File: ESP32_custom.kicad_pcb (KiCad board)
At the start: 4 copper layers, 32 x 42.2 mm, 28 parts, among them J1 TYPE-C-31-M-12, J2 Conn_01x16_Pin, J3 Conn_01x16_Pin, Q1 SS8050, Q2 SS8050, SW1 SW_Push, SW2 SW_Push, U2 ESP32-WROOM-32E 8MB, U3 CH340C, U4 AMS1117-3.3

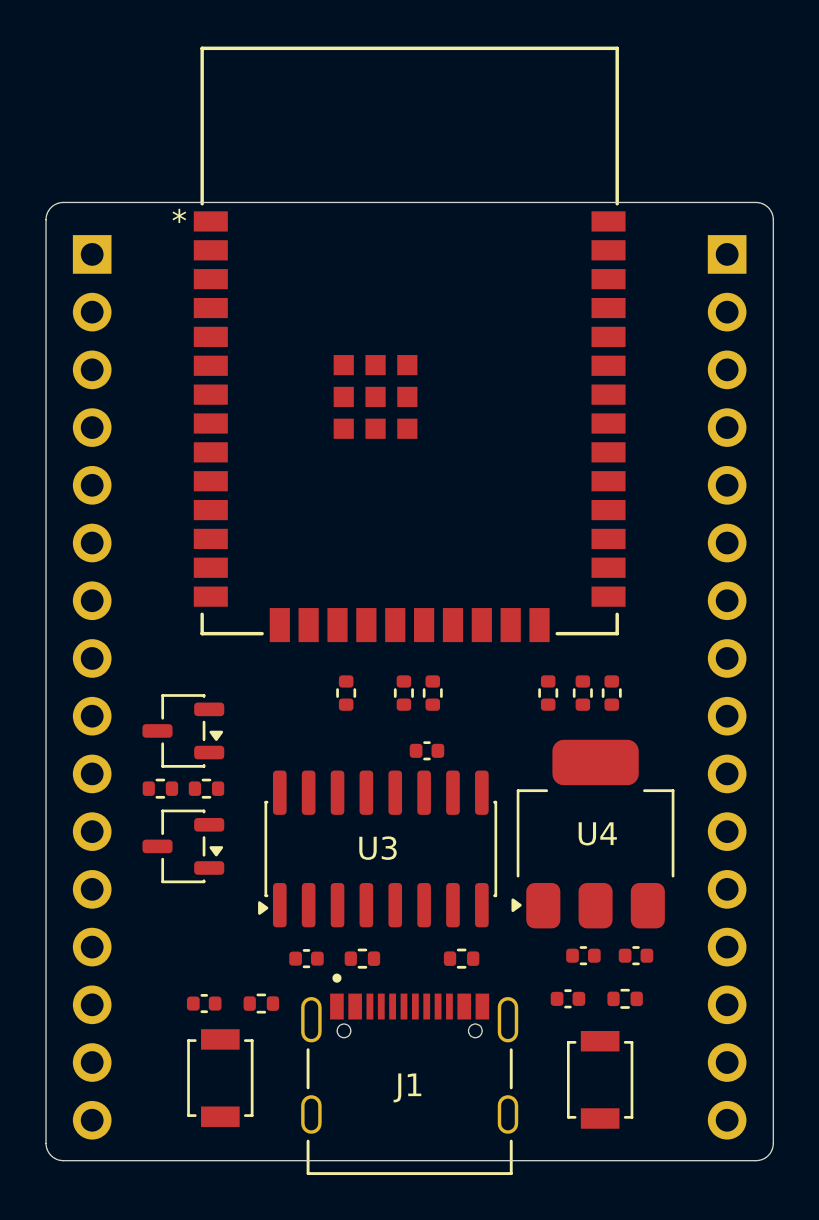
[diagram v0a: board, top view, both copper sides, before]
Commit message: finish routing (DRC fail)
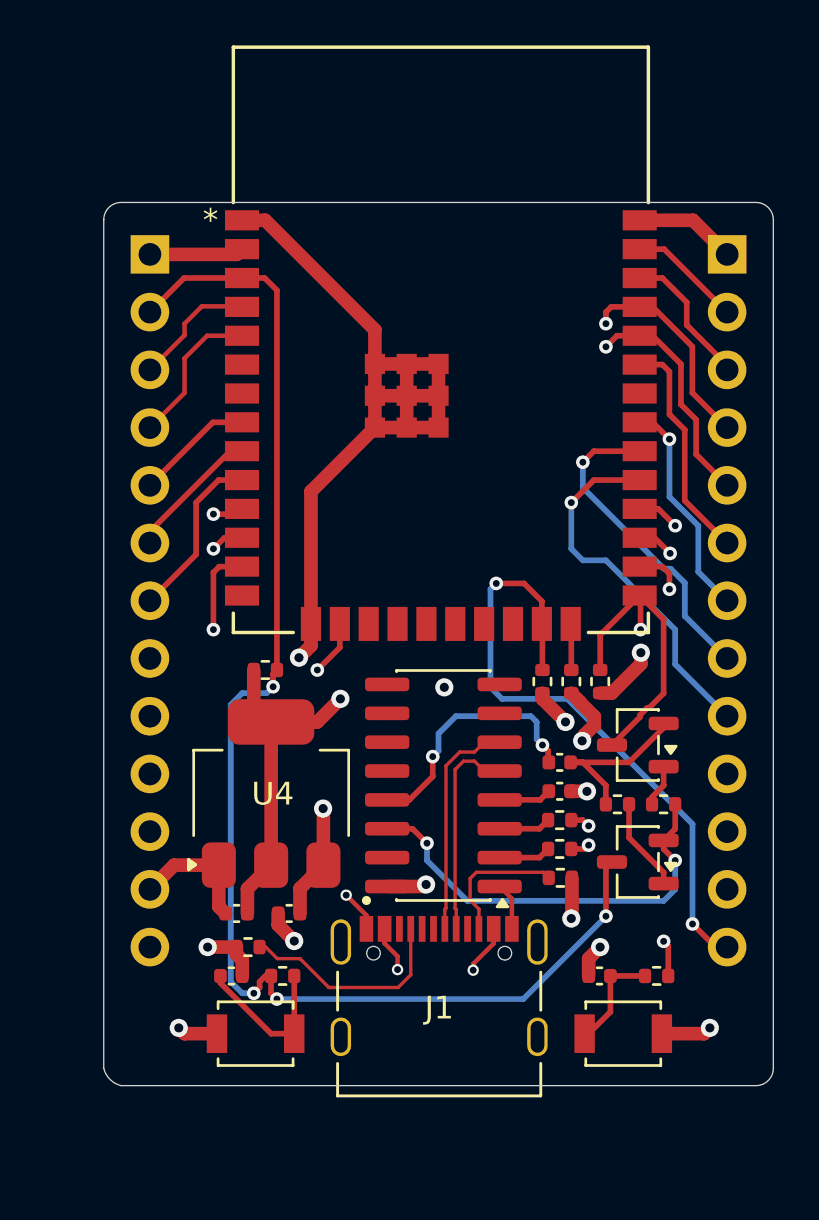
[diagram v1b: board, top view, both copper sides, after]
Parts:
- J2, J3: value Conn_01x16_Pin -> Conn_01x13_Pin; footprint Connector_PinHeader_2.54mm:PinHeader_1x16_P2.54mm_Vertical -> Connector_PinHeader_2.54mm:PinHeader_1x13_P2.54mm_Vertical
- moved R8 20.1 mm to (139.4, 87.2)
- moved R7 20.1 mm to (137.4, 87.2)
- moved Q1 20.0 mm to (138.3, 89.7)
- moved Q2 20.0 mm to (138.3, 84.6)
- moved C3 15.4 mm to (120.7, 92.0)
- moved C4 15.4 mm to (123.0, 92.0)
- moved U4 14.4 mm to (122.2, 86.7)
- moved C2 13.4 mm to (134.9, 86.6)
- moved R2 9.70 mm to (134.9, 89.2), turned to 0 degrees
- moved R1 7.90 mm to (134.9, 87.9), turned to 0 degrees
- moved C1 5.86 mm to (134.9, 85.3), turned to 0 degrees
- moved R11 5.61 mm to (134.9, 90.4)
- moved R12 5.06 mm to (121.2, 93.5)
- moved U3 3.92 mm to (129.8, 86.4), turned to 180 degrees
- moved R9 3.70 mm to (121.9, 81.3), turned to 0 degrees
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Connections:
- J2 pad 10: /IO26 -> /IO14
- J2 pad 11: /IO27 -> /IO13
- J2 pad 12: /IO14 -> GND
- J2 pad 13: /IO12 -> +5V
- J2 pad 5: /IO34 -> /IO32
- J2 pad 6: /IO35 -> /IO33
- J2 pad 7: /IO32 -> /IO25
- J2 pad 8: /IO33 -> /IO26
- J2 pad 9: /IO25 -> /IO27
- J3 pad 10: /IO5 -> /IO17
- J3 pad 11: /IO17 -> /IO16
- J3 pad 12: /IO16 -> /IO4
- J3 pad 13: /IO4 -> /IO15
- J3 pad 7: GND -> /IO19
- J3 pad 8: /IO19 -> /IO18
- J3 pad 9: /IO18 -> /IO5
- U2 pad 14: /IO12 -> unconnected-(U2-IO12-Pad14)
- U2 pad 6: /IO34 -> unconnected-(U2-IO34-Pad6)
- U2 pad 7: /IO35 -> unconnected-(U2-IO35-Pad7)
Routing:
- net GND: track 0.00 -> 68.4 mm, vias 0 -> 11
- net /EN: track 0.00 -> 60.4 mm, vias 0 -> 4
- net /RX: track 0.00 -> 34.4 mm, vias 0 -> 2
- net VCC: track 0.00 -> 33.5 mm, vias 0 -> 4
- net /TX: track 0.00 -> 32.8 mm, vias 0 -> 2
- net /IO0: track 0.00 -> 29.3 mm, vias 0 -> 2
- net /IO15: track 0.00 -> 27.8 mm, vias 0 -> 2
- net /RTS: track 0.00 -> 18.8 mm, vias 0 -> 2
- net /IO4: track 0.00 -> 16.4 mm, vias 0 -> 1
- net /IO5: track 0.00 -> 16.3 mm, vias 0 -> 1
- net /IO16: track 0.00 -> 14.9 mm, vias 0 -> 1
- net /IO18: track 0.00 -> 14.1 mm, vias 0 -> 1
- net /IO17: track 0.00 -> 13.7 mm, vias 0 -> 1
- net /IO13: track 0.00 -> 12.8 mm, vias 0 -> 1
- net /IO14: track 0.00 -> 11.4 mm, vias 0 -> 1
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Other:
- board size 32 x 42.2 mm -> 29.5 x 38.9 mm

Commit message: update schematic. changed to esp32-s3
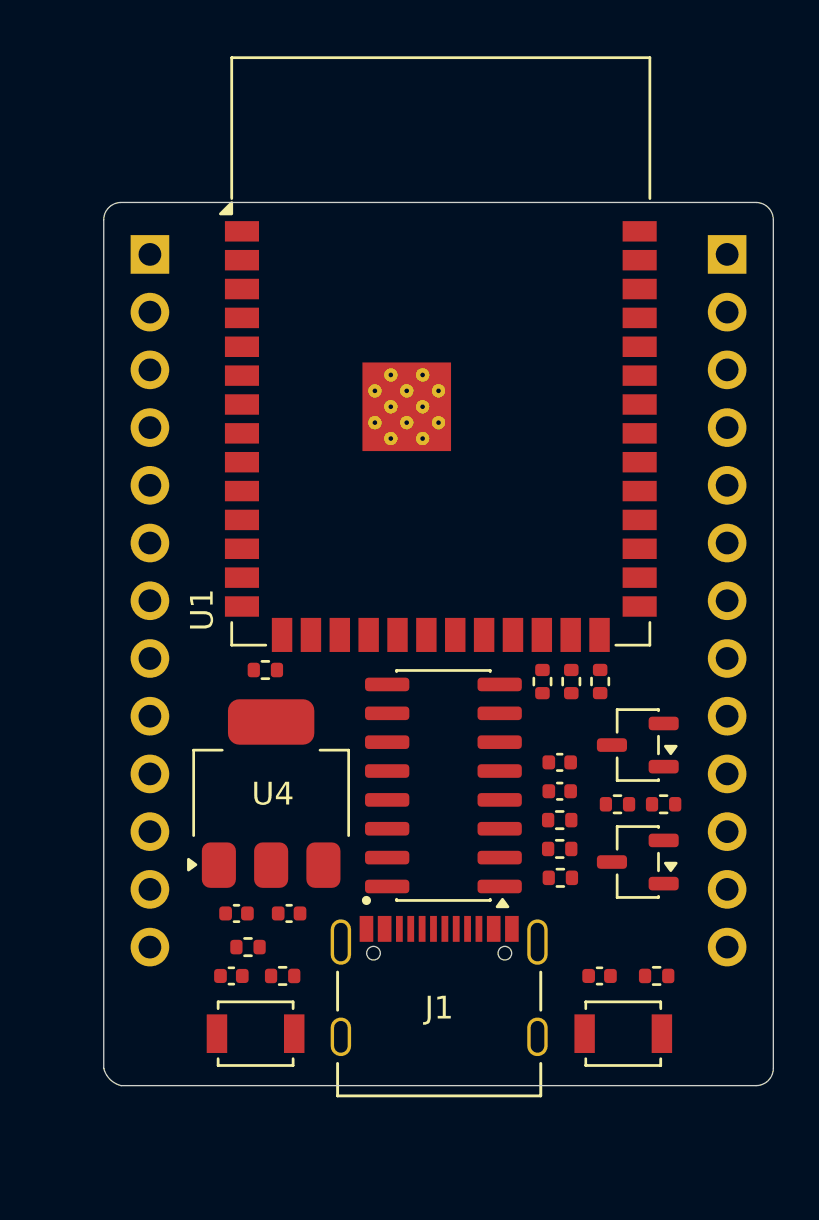
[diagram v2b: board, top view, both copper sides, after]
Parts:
- removed U2: ESP32-WROOM-32E 8MB, KiCADv6:ESP32­WROOM­32E_EXP
- added U1: ESP32-S3-WROOM-1, RF_Module:ESP32-S3-WROOM-1, F.Cu at (129.6, 67.2)
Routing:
- net GND: track 68.4 -> 0.00 mm, vias 11 -> 0
- net /EN: track 60.4 -> 0.00 mm, vias 4 -> 0
- net /RX: track 34.4 -> 0.00 mm, vias 2 -> 0
- net VCC: track 33.5 -> 0.00 mm, vias 4 -> 0
- net /TX: track 32.8 -> 0.00 mm, vias 2 -> 0
- net /IO0: track 29.3 -> 0.00 mm, vias 2 -> 0
- net /IO15: track 27.8 -> 0.00 mm, vias 2 -> 0
- net /RTS: track 18.8 -> 0.00 mm, vias 2 -> 0
- net /IO4: track 16.4 -> 0.00 mm, vias 1 -> 0
- net /IO5: track 16.3 -> 0.00 mm, vias 1 -> 0
- net /IO16: track 14.9 -> 0.00 mm, vias 1 -> 0
- net /IO18: track 14.1 -> 0.00 mm, vias 1 -> 0
- net /IO17: track 13.7 -> 0.00 mm, vias 1 -> 0
- net /IO13: track 12.8 -> 0.00 mm, vias 1 -> 0
- net /IO14: track 11.4 -> 0.00 mm, vias 1 -> 0
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
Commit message: update pcb
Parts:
- removed Q1, Q2: SS8050, Package_TO_SOT_SMD:SOT-23-3
- removed R10, R7, R8, R9: 10K, Resistor_SMD:R_0402_1005Metric
- removed R11, R12: 5.1K, Resistor_SMD:R_0402_1005Metric
- removed U3: CH340C, Package_SO:SOIC-16_3.9x9.9mm_P1.27mm
- added C10: 1uF, Capacitor_SMD:C_0402_1005Metric, F.Cu at (128.3, 90.2)
- added C7: 0u1F, Capacitor_SMD:C_0402_1005Metric, F.Cu at (128.3, 84.2)
- added C8: 10uF, Capacitor_SMD:C_0402_1005Metric, F.Cu at (128.3, 86.2)
- added C9: 10uF, Capacitor_SMD:C_0402_1005Metric, F.Cu at (128.3, 88.2)
- added D1: LESD5D5.0CT1G, LESD5D:TVS_LESD5D5.0CT1G, F.Cu at (137.4, 91.1)
- added D2: LESD5D5.0CT1G, LESD5D:TVS_LESD5D5.0CT1G, F.Cu at (137.4, 93.5)
- added D3: LESD5D5.0CT1G, LESD5D:TVS_LESD5D5.0CT1G, F.Cu at (137.4, 95.8)
- added D4: 1N5819HW-7-F, ul_1N5819HW-7-F:1N5819HW-7-F_DIO, F.Cu at (138.2, 84.1)
- added D5: LED, LED_SMD:LED_0201_0603Metric, F.Cu at (131.2, 84.1)
- added R13: 10K, Resistor_SMD:R_0201_0603Metric, F.Cu at (131.0, 87.6)
- C1, C6: value 100nF -> 0u1F
- C2: value 100nF -> 10uF
- C3, C5: value 10uF -> 0u1F
- R1: value 1K -> 5.1K; footprint Resistor_SMD:R_0402_1005Metric -> Resistor_SMD:R_0201_0603Metric
- R2: value 1K -> 10K; footprint Resistor_SMD:R_0402_1005Metric -> Resistor_SMD:R_0201_0603Metric
- R3: value 470 -> 10K; footprint Resistor_SMD:R_0402_1005Metric -> Resistor_SMD:R_0201_0603Metric
- R4: value 470 -> 10k; footprint Resistor_SMD:R_0402_1005Metric -> Resistor_SMD:R_0201_0603Metric
- R5, R6: value 10K -> 5K1; footprint Resistor_SMD:R_0402_1005Metric -> Resistor_SMD:R_0201_0603Metric
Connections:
- C1 pad 1: Net-(U3-~{DTR}) -> +5V
- C1 pad 2: /DTR -> GND
- C2 pad 1: Net-(U3-V3) -> +5V
- C4 pad 1: GND -> VCC
- C4 pad 2: +5V -> GND
- C5 pad 1: Net-(C5-Pad1) -> /GPIO0
- C6 pad 1: Net-(C6-Pad1) -> /CHIP_PU
- J1 pad A4_B9: +5V -> VBUS
- J1 pad A5: /CC1 -> Net-(J1-CC1)
- J1 pad B4_A9: +5V -> VBUS
- J1 pad B5: /CC2 -> Net-(J1-CC2)
- J1 pad S1: unconnected-(J1-SHIELD-PadS1)_3 -> GND
- J1 pad S2: unconnected-(J1-SHIELD-PadS1)_2 -> GND
- J1 pad S3: unconnected-(J1-SHIELD-PadS1) -> GND
- J1 pad S4: unconnected-(J1-SHIELD-PadS1)_1 -> GND
- J2 pad 2: /EN -> /CHIP_PU
- R1 pad 1: Net-(U3-RXD) -> VCC
- R1 pad 2: /TX -> Net-(D5-A)
- R2 pad 1: Net-(U3-TXD) -> /CHIP_PU
- R2 pad 2: /RX -> /ESP_3V3
- R3 pad 1: /IO0 -> VCC
- R3 pad 2: Net-(C5-Pad1) -> /GPIO0
- R4 pad 1: /EN -> VCC
- R4 pad 2: Net-(C6-Pad1) -> /CHIP_PU
- R5 pad 1: /IO0 -> Net-(J1-CC2)
- R5 pad 2: VCC -> GND
- R6 pad 1: /IO2 -> Net-(J1-CC1)
- SW1 pad 1: Net-(C5-Pad1) -> /GPIO0
- SW2 pad 1: Net-(C6-Pad1) -> /CHIP_PU
- U1 pad 1: Net-(U1-GND-Pad1) -> GND
- U1 pad 10: unconnected-(U1-IO17-Pad10) -> /GPIO17
- U1 pad 11: unconnected-(U1-IO18-Pad11) -> /GPIO18
- U1 pad 12: unconnected-(U1-IO8-Pad12) -> /GPIO08
- U1 pad 13: unconnected-(U1-USB_D--Pad13) -> /D-
- U1 pad 14: unconnected-(U1-USB_D+-Pad14) -> /D+
- U1 pad 15: unconnected-(U1-IO3-Pad15) -> /GPIO03
- U1 pad 16: unconnected-(U1-IO46-Pad16) -> /GPIO46
- U1 pad 17: unconnected-(U1-IO9-Pad17) -> /GPIO09
- U1 pad 18: unconnected-(U1-IO10-Pad18) -> /GPIO10
- U1 pad 19: unconnected-(U1-IO11-Pad19) -> /GPIO11
- U1 pad 2: unconnected-(U1-3V3-Pad2) -> /ESP_3V3
- U1 pad 20: unconnected-(U1-IO12-Pad20) -> /GPIO12
- U1 pad 21: unconnected-(U1-IO13-Pad21) -> /GPIO13
- U1 pad 22: unconnected-(U1-IO14-Pad22) -> /GPIO14
- U1 pad 23: unconnected-(U1-IO21-Pad23) -> /GPIO21
- U1 pad 24: unconnected-(U1-IO47-Pad24) -> /GPIO47
- U1 pad 25: unconnected-(U1-IO48-Pad25) -> /GPIO48
- U1 pad 26: unconnected-(U1-IO45-Pad26) -> /GPIO45
- U1 pad 27: unconnected-(U1-IO0-Pad27) -> /GPIO0
- U1 pad 28: unconnected-(U1-IO35-Pad28) -> /GPIO35
- U1 pad 29: unconnected-(U1-IO36-Pad29) -> /GPIO36
- U1 pad 3: unconnected-(U1-EN-Pad3) -> /CHIP_PU
- U1 pad 30: unconnected-(U1-IO37-Pad30) -> /GPIO37
- U1 pad 31: unconnected-(U1-IO38-Pad31) -> /GPIO38
- U1 pad 32: unconnected-(U1-IO39-Pad32) -> /GPIO39
- U1 pad 33: unconnected-(U1-IO40-Pad33) -> /GPIO40
- U1 pad 34: unconnected-(U1-IO41-Pad34) -> /GPIO41
- U1 pad 35: unconnected-(U1-IO42-Pad35) -> /GPIO42
- U1 pad 36: unconnected-(U1-RXD0-Pad36) -> /RX
- U1 pad 37: unconnected-(U1-TXD0-Pad37) -> /TX
- U1 pad 38: unconnected-(U1-IO2-Pad38) -> /GPIO02
- U1 pad 39: unconnected-(U1-IO1-Pad39) -> /GPIO01
- U1 pad 4: unconnected-(U1-IO4-Pad4) -> /GPIO04
- U1 pad 40: Net-(U1-GND-Pad1) -> GND
- U1 pad 41: Net-(U1-GND-Pad1) -> GND
- U1 pad 5: unconnected-(U1-IO5-Pad5) -> /GPIO05
- U1 pad 6: unconnected-(U1-IO6-Pad6) -> /GPIO06
- U1 pad 7: unconnected-(U1-IO7-Pad7) -> /GPIO07
- U1 pad 8: unconnected-(U1-IO15-Pad8) -> /GPIO15
- U1 pad 9: unconnected-(U1-IO16-Pad9) -> /GPIO16

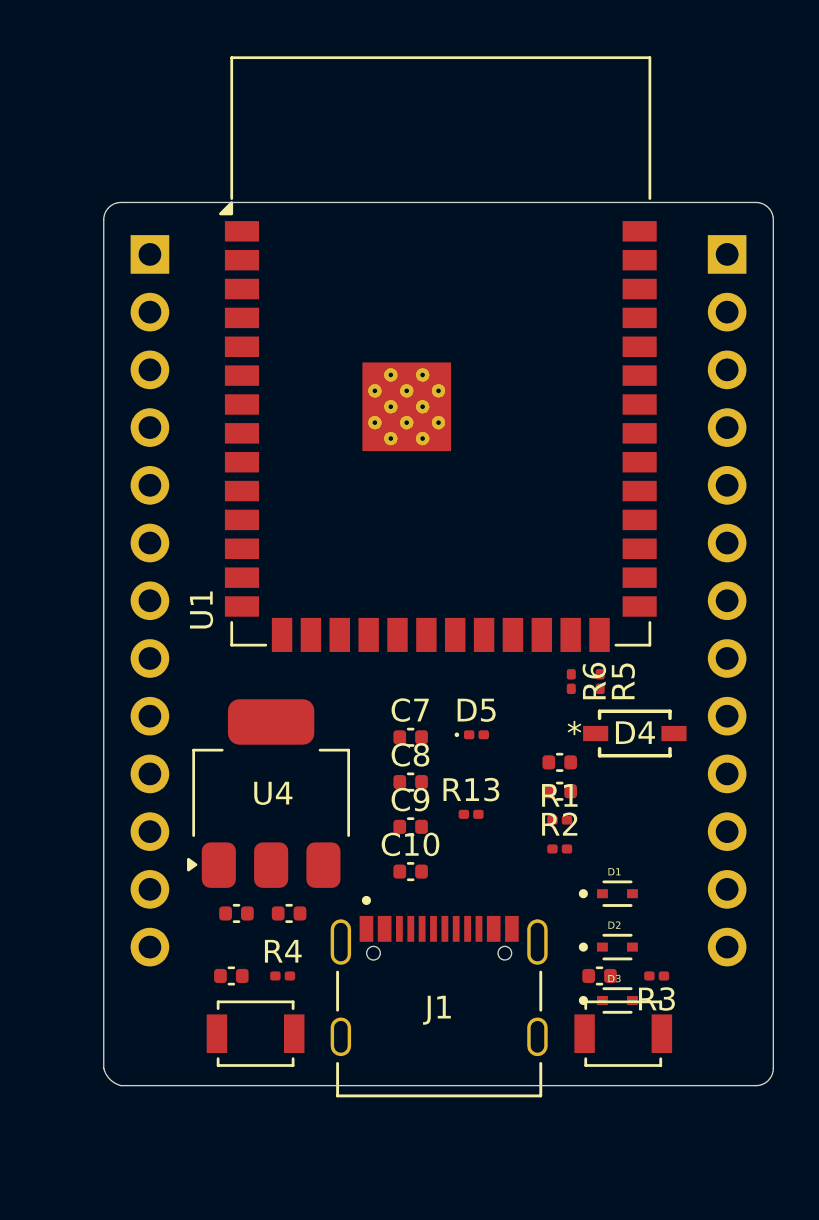
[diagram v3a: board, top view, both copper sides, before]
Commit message: arrange components and update pin header label
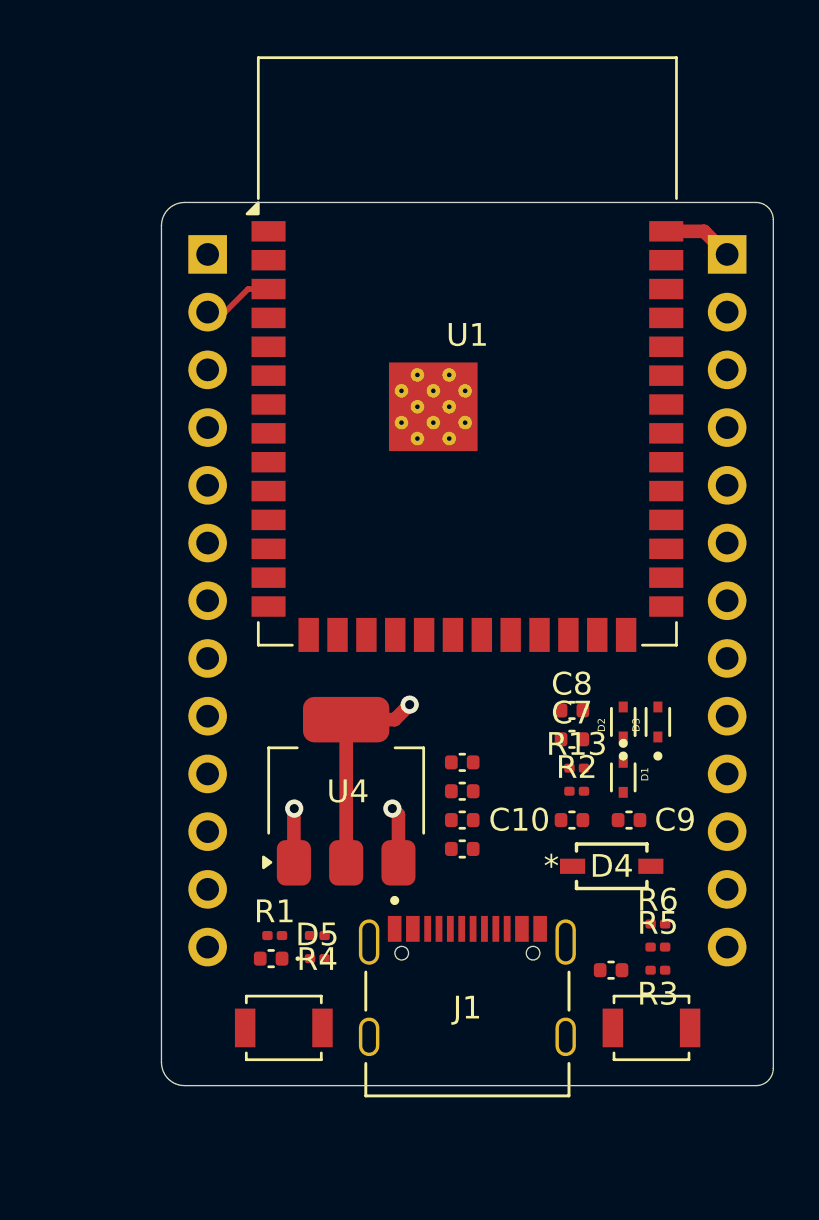
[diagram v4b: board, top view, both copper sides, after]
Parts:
- moved R1 13.5 mm to (122.3, 93.0)
- moved D3 12.4 mm to (139.2, 83.6), turned to 90 degrees
- moved D5 12.1 mm to (124.2, 94.0)
- moved R5 12.0 mm to (139.2, 93.5), turned to 0 degrees
- moved R6 11.3 mm to (139.2, 92.5), turned to 0 degrees
- moved C3 11.3 mm to (130.6, 86.6), turned to 0 degrees
- moved C4 10.1 mm to (130.6, 85.3)
- moved D2 9.91 mm to (137.7, 83.6), turned to 90 degrees
- moved C9 9.61 mm to (137.9, 87.9), turned to 180 degrees
- moved C8 7.77 mm to (135.4, 83.1)
- moved C10 7.45 mm to (135.4, 87.9)
- moved C7 7.10 mm to (135.4, 84.3)
- moved D4 5.93 mm to (137.2, 89.9)
- moved D1 5.12 mm to (137.7, 86.0), turned to -90 degrees
- moved R13 5.07 mm to (135.6, 85.6)
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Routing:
- net VCC: track 0.00 -> 9.37 mm, vias 0 -> 1
- net GND: track 0.00 -> 5.49 mm, vias 0 -> 1
- net /CHIP_PU: track 0.00 -> 3.10 mm
- net +5V: track 0.00 -> 2.50 mm, vias 0 -> 1
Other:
- board size 29.5 x 38.9 mm -> 26.9 x 38.9 mm
